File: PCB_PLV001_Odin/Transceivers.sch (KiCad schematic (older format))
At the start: 26 parts, among them J2 IMU, J3 INS, U10 SN65HVD232, U8 MAX3221, U9 MAX3221

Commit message: Work on Odin and Yggdrasil, create Heimdal.
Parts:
- removed C23: 0.1uF, symbol Device:C
- removed U10: SN65HVD232, Package_SO:SOIC-8_3.9x4.9mm_P1.27mm, symbol Interface_CAN_LIN:SN65HVD232
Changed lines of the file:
@@
 232_1_VALID
-$Comp
-L Interface_CAN_LIN:SN65HVD232 U10
-U 1 1 5FBD4A6A
-P 8200 2200
-F 0 "U10" H 7950 2450 50  0000 C CNN
-F 1 "SN65HVD232" H 7850 1850 50  0000 C CNN
-F 2 "Package_SO:SOIC-8_3.9x4.9mm_P1.27mm" H 8200 1700 50  0001 C CNN
-F 3 "http://www.ti.com/lit/ds/symlink/sn65hvd230.pdf" H 8100 2600 50  0001 C CNN
-	1    8200 2200
-	1    0    0    -1
-$EndComp
-Text HLabel 7750 2200 0    50   Output ~ 0
-CAN_RX
-Text HLabel 7750 2100 0    50   Input ~ 0
-CAN_TX
-Text HLabel 8650 2200 2    50   BiDi ~ 0
-CANH
-Text HLabel 8650 2300 2    50   BiDi ~ 0
-CANL
-Wire Wire Line
-	8650 2300 8600 2300
-Wire Wire Line
-	8600 2200 8650 2200
-Wire Wire Line
-	7750 2100 7800 2100
-Wire Wire Line
-	7800 2200 7750 2200
-$Comp
-L power:+3.3V #PWR0126
-U 1 1 5FBDCED0
-P 8200 1850
-F 0 "#PWR0126" H 8200 1700 50  0001 C CNN
-F 1 "+3.3V" H 8215 2023 50  0000 C CNN
-F 2 "" H 8200 1850 50  0001 C CNN
-F 3 "" H 8200 1850 50  0001 C CNN
-	1    8200 1850
-	1    0    0    -1
-$EndComp
-Wire Wire Line
-	8200 1850 8200 1900
-Wire Wire Line
-	8200 2600 8200 2650
-$Comp
-L power:GND #PWR?
-U 1 1 5FBE0C17
-P 8200 2650
-AR Path="/5FBE0C17" Ref="#PWR?"  Part="1"
-AR Path="/5FB797DD/5FBE0C17" Ref="#PWR0127"  Part="1"
-F 0 "#PWR0127" H 8200 2400 50  0001 C CNN
-F 1 "GND" H 8205 2477 50  0000 C CNN
-F 2 "" H 8200 2650 50  0001 C CNN
-F 3 "" H 8200 2650 50  0001 C CNN
-	1    8200 2650
-	1    0    0    -1
-$EndComp
-$Comp
-L Device:C C?
-U 1 1 5FBE4AE7
-P 9050 2250
-AR Path="/5FBE4AE7" Ref="C?"  Part="1"
-AR Path="/5FB797DD/5FBE4AE7" Ref="C23"  Part="1"
-F 0 "C23" H 9165 2296 50  0000 L CNN
-F 1 "0.1uF" H 9165 2205 50  0000 L CNN
-F 2 "" H 9088 2100 50  0001 C CNN
-F 3 "~" H 9050 2250 50  0001 C CNN
-	1    9050 2250
-	1    0    0    -1
-$EndComp
-$Comp
-L power:GND #PWR?
-U 1 1 5FBE4AF1
-P 9050 2450
-AR Path="/5FBE4AF1" Ref="#PWR?"  Part="1"
-AR Path="/5FB797DD/5FBE4AF1" Ref="#PWR0128"  Part="1"
-F 0 "#PWR0128" H 9050 2200 50  0001 C CNN
-F 1 "GND" H 9055 2277 50  0000 C CNN
-F 2 "" H 9050 2450 50  0001 C CNN
-F 3 "" H 9050 2450 50  0001 C CNN
-	1    9050 2450
-	1    0    0    -1
-$EndComp
-Wire Wire Line
-	9050 2400 9050 2450
-$Comp
-L power:+3.3V #PWR?
-U 1 1 5FBE4AFC
-P 9050 2050
-AR Path="/5FBE4AFC" Ref="#PWR?"  Part="1"
-AR Path="/5FB797DD/5FBE4AFC" Ref="#PWR0129"  Part="1"
-F 0 "#PWR0129" H 9050 1900 50  0001 C CNN
-F 1 "+3.3V" H 9065 2223 50  0000 C CNN
-F 2 "" H 9050 2050 50  0001 C CNN
-F 3 "" H 9050 2050 50  0001 C CNN
-	1    9050 2050
-	1    0    0    -1
-$EndComp
-Wire Wire Line
-	9050 2050 9050 2100
 $Comp
 L Connector_Generic:Conn_01x05 J2

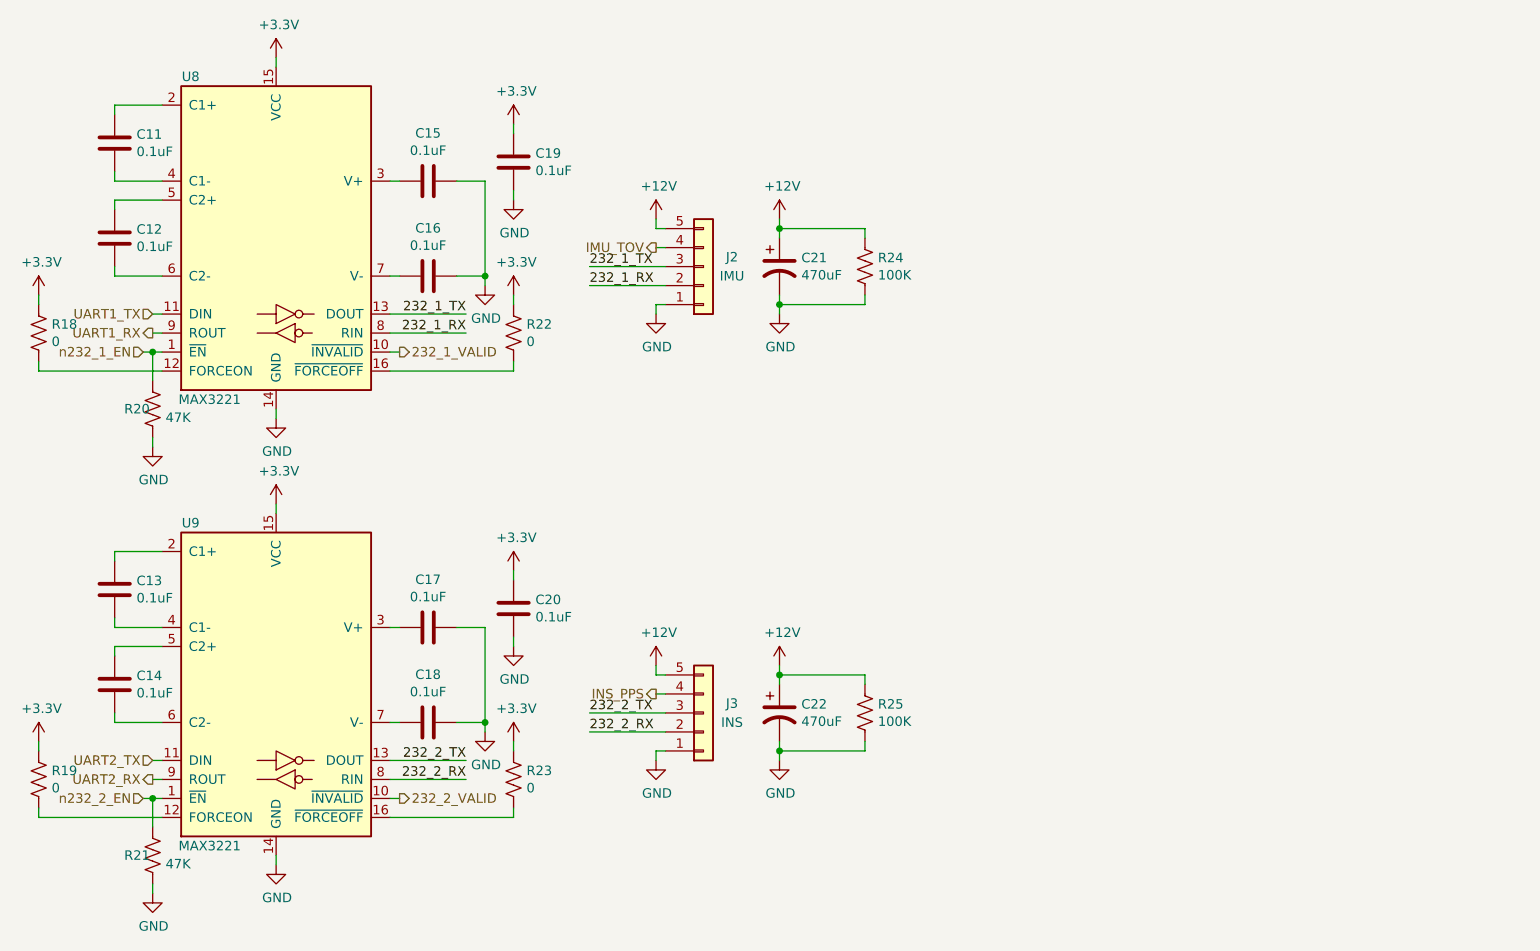
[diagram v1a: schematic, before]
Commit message: Spec all current parts for Odin
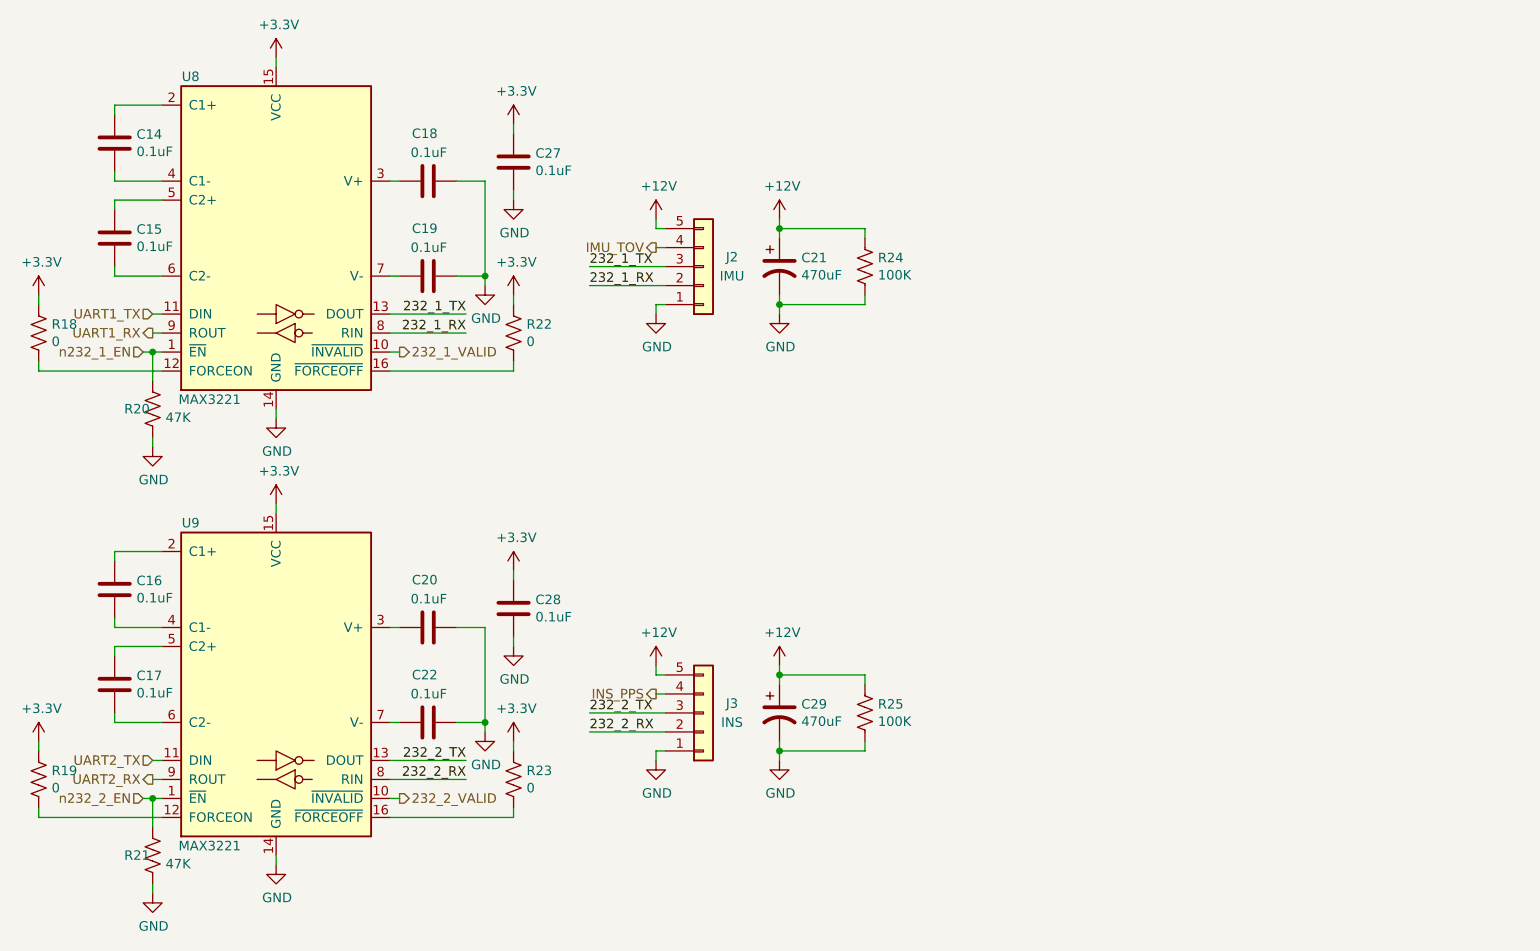
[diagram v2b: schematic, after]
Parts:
- removed C11, C12, C13: 0.1uF, symbol Device:C
- removed C22: 470uF, symbol Device:CP1
- added C22, C27, C28: 0.1uF, Capacitor_SMD:C_0603_1608Metric_Pad1.05x0.95mm_HandSolder, symbol Device:C
- added C29: 470uF, Capacitor_THT:CP_Radial_D10.0mm_P5.00mm, symbol Device:CP1
- C14, C15, C16, C17, C18, C19, C20: footprint (none) -> Capacitor_SMD:C_0603_1608Metric_Pad1.05x0.95mm_HandSolder; MFPN (none) -> CC0603KRX7R8BB104
- C21: footprint (none) -> Capacitor_THT:CP_Radial_D10.0mm_P5.00mm; MFPN (none) -> 25WXA470MEFC10X9
- J2, J3: footprint (none) -> Connector_Molex:Molex_Micro-Fit_3.0_43650-0500_1x05_P3.00mm_Horizontal; MFPN (none) -> 0436500500
- R18, R19, R22, R23: footprint (none) -> Resistor_SMD:R_0603_1608Metric_Pad1.05x0.95mm_HandSolder
- R20, R21: footprint (none) -> Resistor_SMD:R_0603_1608Metric_Pad1.05x0.95mm_HandSolder; MFPN (none) -> RMCF0603FT47K0
- R24, R25: footprint (none) -> Resistor_SMD:R_0603_1608Metric_Pad1.05x0.95mm_HandSolder; MFPN (none) -> RMCF0603FG100K
- U8, U9: footprint (none) -> Package_SO:TSSOP-16_4.4x5mm_P0.65mm; MFPN (none) -> MAX3221CPWR
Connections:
- net +12V: now also C29.1
- net +3V3: now also C27.1, C28.1; no longer C19.1, C20.1
- net GND: now also C18.2, C22.2, C27.2, C28.2, C29.2; no longer C15.1, C16.1, C17.1, C18.1
- net at U8.2 (C1+): now also C14.1
- net at C15.2: now also U8.6 (C2-); no longer U8.3 (V+)
- net at U8.4 (C1-): now also C14.2
- net at U8.5 (C2+): now also C15.1
- net at C16.2: now also U9.4 (C1-); no longer U8.7 (V-)
- net at U9.2 (C1+): now also C16.1
- net at U9.3 (V+): now also C20.1; no longer C17.2
- net at U9.5 (C2+): now also C17.1; no longer C14.1
- net at U9.6 (C2-): now also C17.2; no longer C14.2
- net at U9.7 (V-): now also C22.1; no longer C18.2
- new net: C19.1, U8.7 (V-)
- new net: C18.1, U8.3 (V+)
